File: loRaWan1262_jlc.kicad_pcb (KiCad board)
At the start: 2 copper layers, 63.5 x 22.9 mm, 87 parts, among them J1 BAT, J2 Feather_BOT, J3 Feather_TOP, J4 SWD, J5 USB_B_Micro, Q1 MMBT3904, SW1 USER, SW2 RESET, SW3 BOOT, U1 MCP73831-2-OT, U10 USBLC6-2SC6, U2 STC3100, U3 XC6206, U4 MAX40200AUK, U5 MAX40200AUK, U6 TPS63001, U7 DRF1262x, U8 ATECC608A-SSHDA, U9 STM32L073CZTx, Y1 8MHz, Y2 32.768kHz

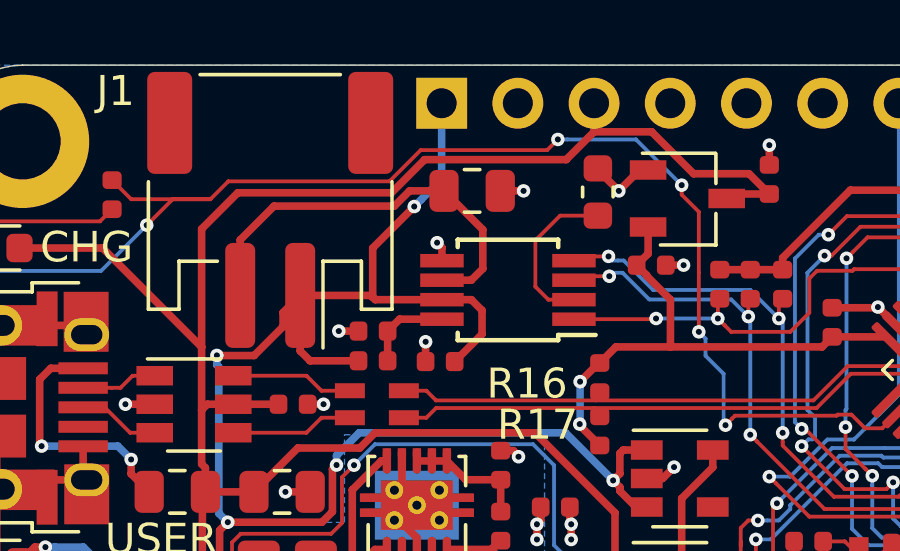
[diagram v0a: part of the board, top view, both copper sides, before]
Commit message: PCB REV B0 * Fix STC3100 grounding * Make R16,R17 DNP by default * Bump Bot Silk to REVB0
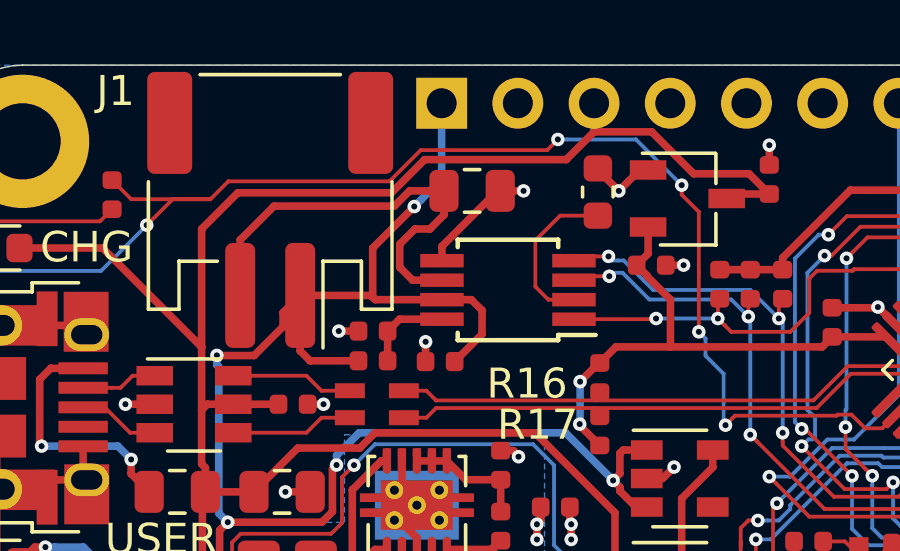
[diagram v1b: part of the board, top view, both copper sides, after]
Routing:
- net GND: track 89.9 -> 92.4 mm, vias 50 -> 49
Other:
- board text added: "REV B0"
- board text removed: "REV A0"
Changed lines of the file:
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@@
     (thickness 1.6)
     (drawings 55)
-    (tracks 1268)
+    (tracks 1271)
     (zones 0)
     (modules 87)
@@
     (visible_elements 7FFFFF7F)
     (pcbplotparams
-      (layerselection 0x3c100_7ffffffe)
+      (layerselection 0x010fc_ffffffff)
       (usegerberextensions false)
       (usegerberattributes false)
@@
     (effects (font (size 1.016 1.016) (thickness 0.254)))
   )
-  (gr_text "REV A0" (at 176.276 85.09 90) (layer B.SilkS)
+  (gr_text "REV B0" (at 176.276 85.09 90) (layer B.SilkS)
     (effects (font (size 1.016 1.016) (thickness 0.254)) (justify mirror))
   )
@@
   (segment (start 120.5865 96.585) (end 120.47981 96.47831) (width 0.254) (layer F.Cu) (net 2))
   (segment (start 119.697803 96.703309) (end 119.922802 96.47831) (width 0.254) (layer B.Cu) (net 2))
-  (via (at 130.6576 83.6422) (size 0.45) (drill 0.2) (layers F.Cu B.Cu) (net 2))
-  (segment (start 130.8198 84.242) (end 130.8198 83.8044) (width 0.254) (layer F.Cu) (net 2))
-  (segment (start 130.8198 83.8044) (end 130.6576 83.6422) (width 0.254) (layer F.Cu) (net 2))
   (via (at 127.381 86.5886) (size 0.45) (drill 0.2) (layers F.Cu B.Cu) (net 2))
   (segment (start 128.039 86.5886) (end 127.381 86.5886) (width 0.254) (layer F.Cu) (net 2))
@@
   (segment (start 130.2742 87.6046) (end 130.2742 86.9466) (width 0.254) (layer F.Cu) (net 2))
   (segment (start 130.2742 86.9466) (end 130.2766 86.9442) (width 0.254) (layer F.Cu) (net 2))
+  (segment (start 132.6678 81.915) (end 132.7635 81.915) (width 0.254) (layer F.Cu) (net 2))
+  (segment (start 130.8198 83.763) (end 132.6678 81.915) (width 0.254) (layer F.Cu) (net 2))
+  (segment (start 130.8198 84.242) (end 130.8198 83.763) (width 0.254) (layer F.Cu) (net 2))
   (segment (start 122.936 91.948) (end 124.5535 91.948) (width 0.254) (layer F.Cu) (net 3) (status 30))
   (segment (start 123.001 89.027) (end 123.865 89.027) (width 0.254) (layer F.Cu) (net 3) (status 20))
@@
   (segment (start 124.095 83.55) (end 124.095 85.4) (width 0.254) (layer F.Cu) (net 23) (status 20))
   (segment (start 129.740836 81.915) (end 130.8885 81.915) (width 0.254) (layer F.Cu) (net 23))
-  (segment (start 131.7988 84.892) (end 132.1816 84.5092) (width 0.254) (layer F.Cu) (net 23))
-  (segment (start 130.8198 84.892) (end 131.7988 84.892) (width 0.254) (layer F.Cu) (net 23))
-  (segment (start 132.1816 83.2081) (end 130.8885 81.915) (width 0.254) (layer F.Cu) (net 23))
-  (segment (start 132.1816 84.5092) (end 132.1816 83.2081) (width 0.254) (layer F.Cu) (net 23))
+  (segment (start 129.8408 84.892) (end 129.413 84.4642) (width 0.254) (layer F.Cu) (net 23))
+  (segment (start 130.8198 84.892) (end 129.8408 84.892) (width 0.254) (layer F.Cu) (net 23))
+  (segment (start 129.413 84.4642) (end 129.413 83.693) (width 0.254) (layer F.Cu) (net 23))
+  (segment (start 130.8885 82.715) (end 130.4185 83.185) (width 0.254) (layer F.Cu) (net 23))
+  (segment (start 130.8885 81.915) (end 130.8885 82.715) (width 0.254) (layer F.Cu) (net 23))
+  (segment (start 129.921 83.185) (end 129.413 83.693) (width 0.254) (layer F.Cu) (net 23))
+  (segment (start 130.4185 83.185) (end 129.921 83.185) (width 0.254) (layer F.Cu) (net 23))
   (segment (start 130.81 99.314) (end 132.588 97.536) (width 0.127) (layer B.Cu) (net 24) (status 10))
   (via (at 140.7795 97.028) (size 0.45) (drill 0.2) (layers F.Cu B.Cu) (net 24))

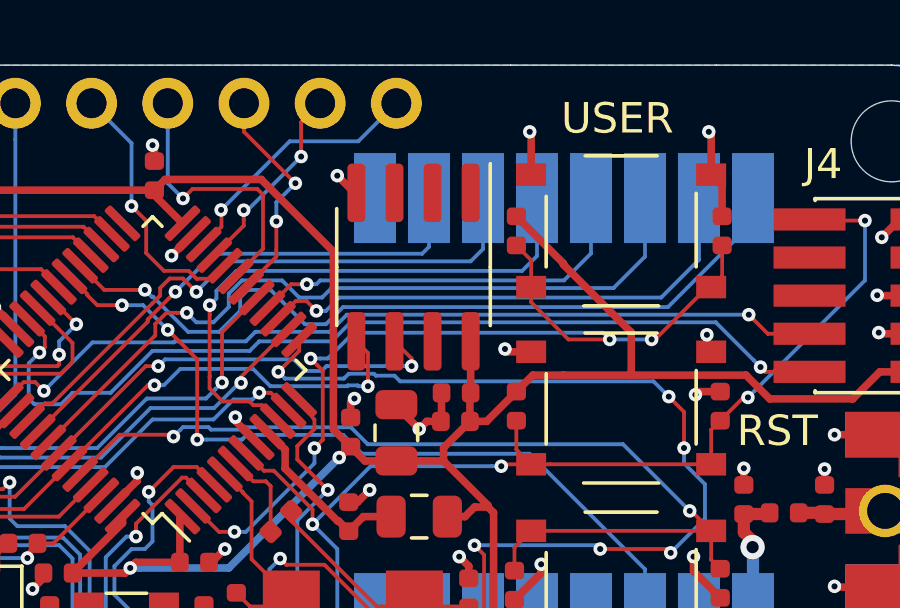
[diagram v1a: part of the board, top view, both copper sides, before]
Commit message: PCB REV C0 * Make U8 footprint capable of crypto and fram device * Minor updates to schematic * Minor updates to doc prints * Update bot silk to REV C0
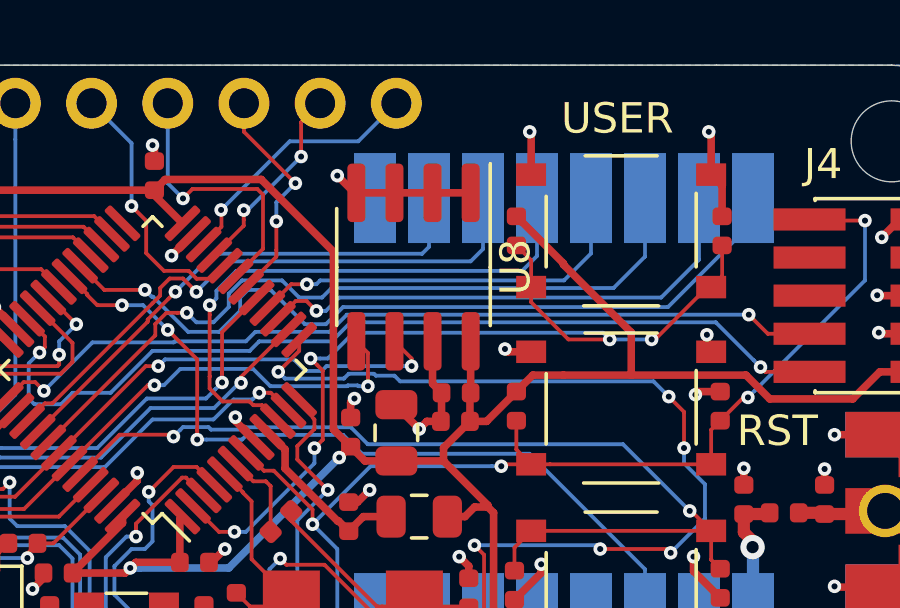
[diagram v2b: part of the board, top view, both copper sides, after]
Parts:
- removed REF**: KiCad-Logo2_5mm_SilkScreen, Symbol:KiCad-Logo2_5mm_SilkScreen
- U8: value ATECC608A-SSHDA -> SOIC8-CRYPTO-FRAM; footprint jlcpcb_smt:SOIC-8_3.9x4.9mm_P1.27mm -> Package_SO:SOIC-8_3.9x4.9mm_P1.27mm
- turned U8 to 270 degrees
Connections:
- U8 pad 1: (no net) -> GND
- U8 pad 2: (no net) -> GND
- U8 pad 3: (no net) -> GND
- U8 pad 7: (no net) -> GND
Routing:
- net GND: track 92.4 -> 98.0 mm
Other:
- board text added: "LoRaWAN Feather svcguy 11/19 REV C0"
- board text added: "REV C0"
- board text removed: "LoRaWAN Feather svcguy 11/19 REV A0"
- board text removed: "REV B0"
